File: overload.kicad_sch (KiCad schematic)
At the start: 50 parts, among them J1 AudioPlug2, J2 AudioPlug4, Q1 NPN, Q10 NPN, Q11 PNP, Q12 PNP, Q13 NPN, Q14 NPN, Q15 PNP, Q16 PNP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

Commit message: feat: updated footprint tables
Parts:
- C1, C2: footprint (none) -> Capacitor_SMD:C_0603_1608Metric
- R1, R10, R11, R12, R13, R14, R15, R16, R17, R18, R19, R2, R20, R21, R22, R23, R3, R4, R5, R6, R7, R8, R9: footprint (none) -> Resistor_SMD:R_0603_1608Metric
- U1: footprint (none) -> NE5532DR:D8
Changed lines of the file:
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@@
 			)
 		)
-		(property "Footprint" ""
+		(property "Footprint" "Resistor_SMD:R_0603_1608Metric"
 			(at 145.542 124.46 90)
 			(effects
@@
 			)
 		)
-		(property "Footprint" ""
+		(property "Footprint" "Resistor_SMD:R_0603_1608Metric"
 			(at 223.012 99.06 90)
 			(effects
@@
 			)
 		)
-		(property "Footprint" ""
+		(property "Footprint" "Resistor_SMD:R_0603_1608Metric"
 			(at 214.122 45.72 90)
 			(effects
@@
 			)
 		)
-		(property "Footprint" ""
+		(property "Footprint" "Resistor_SMD:R_0603_1608Metric"
 			(at 242.062 96.52 90)
 			(effects
@@
 			)
 		)
-		(property "Footprint" ""
+		(property "Footprint" "Capacitor_SMD:C_0603_1608Metric"
 			(at 94.2848 96.52 0)
 			(effects
@@
 			)
 		)
-		(property "Footprint" ""
+		(property "Footprint" "Capacitor_SMD:C_0603_1608Metric"
 			(at 99.06 71.4248 0)
 			(effects
@@
 			)
 		)
-		(property "Footprint" ""
+		(property "Footprint" "NE5532DR:D8"
 			(at 118.11 96.52 0)
 			(effects
@@
 			)
 		)
-		(property "Footprint" ""
+		(property "Footprint" "Resistor_SMD:R_0603_1608Metric"
 			(at 85.09 109.728 90)
 			(effects
@@
 			)
 		)
-		(property "Footprint" ""
+		(property "Footprint" "Resistor_SMD:R_0603_1608Metric"
 			(at 153.162 58.42 90)
 			(effects
@@
 			)
 		)
-		(property "Footprint" ""
+		(property "Footprint" "Resistor_SMD:R_0603_1608Metric"
 			(at 242.062 83.82 90)
 			(effects
@@
 			)
 		)
-		(property "Footprint" ""
+		(property "Footprint" "NE5532DR:D8"
 			(at 43.18 123.19 0)
 			(effects
@@
 			)
 		)
-		(property "Footprint" ""
+		(property "Footprint" "Resistor_SMD:R_0603_1608Metric"
 			(at 85.09 84.328 90)
 			(effects
@@
 			)
 		)
-		(property "Footprint" ""
+		(property "Footprint" "Resistor_SMD:R_0603_1608Metric"
 			(at 197.612 125.73 90)
 			(effects
@@
 			)
 		)
-		(property "Footprint" ""
+		(property "Footprint" "Resistor_SMD:R_0603_1608Metric"
 			(at 223.012 86.36 90)
 			(effects
@@
 			)
 		)
-		(property "Footprint" ""
+		(property "Footprint" "Resistor_SMD:R_0603_1608Metric"
 			(at 136.652 78.74 90)
 			(effects
@@
 			)
 		)
-		(property "Footprint" ""
+		(property "Footprint" "Resistor_SMD:R_0603_1608Metric"
 			(at 257.302 93.98 90)
 			(effects
@@
 			)
 		)
-		(property "Footprint" ""
+		(property "Footprint" "Resistor_SMD:R_0603_1608Metric"
 			(at 162.052 86.36 90)
 			(effects
@@
 			)
 		)
-		(property "Footprint" ""
+		(property "Footprint" "Resistor_SMD:R_0603_1608Metric"
 			(at 93.472 90.17 90)
 			(effects
@@
 			)
 		)
-		(property "Footprint" ""
+		(property "Footprint" "Resistor_SMD:R_0603_1608Metric"
 			(at 162.052 124.46 90)
 			(effects
@@
 			)
 		)
-		(property "Footprint" ""
+		(property "Footprint" "Resistor_SMD:R_0603_1608Metric"
 			(at 257.302 86.36 90)
 			(effects
@@
 			)
 		)
-		(property "Footprint" ""
+		(property "Footprint" "Resistor_SMD:R_0603_1608Metric"
 			(at 105.41 84.328 90)
 			(effects
@@
 			)
 		)
-		(property "Footprint" ""
+		(property "Footprint" "Resistor_SMD:R_0603_1608Metric"
 			(at 145.542 86.36 90)
 			(effects
@@
 			)
 		)
-		(property "Footprint" ""
+		(property "Footprint" "Resistor_SMD:R_0603_1608Metric"
 			(at 169.672 102.87 90)
 			(effects
@@
 			)
 		)
-		(property "Footprint" ""
+		(property "Footprint" "NE5532DR:D8"
 			(at 63.5 93.98 0)
 			(effects
@@
 			)
 		)
-		(property "Footprint" ""
+		(property "Footprint" "Resistor_SMD:R_0603_1608Metric"
 			(at 177.8 98.298 90)
 			(effects
@@
 			)
 		)
-		(property "Footprint" ""
+		(property "Footprint" "Resistor_SMD:R_0603_1608Metric"
 			(at 214.122 125.73 90)
 			(effects
@@
 			)
 		)
-		(property "Footprint" ""
+		(property "Footprint" "Resistor_SMD:R_0603_1608Metric"
 			(at 105.41 109.728 90)
 			(effects
@@
 			)
 		)
-		(property "Footprint" ""
+		(property "Footprint" "Resistor_SMD:R_0603_1608Metric"
 			(at 206.502 67.31 90)
 			(effects

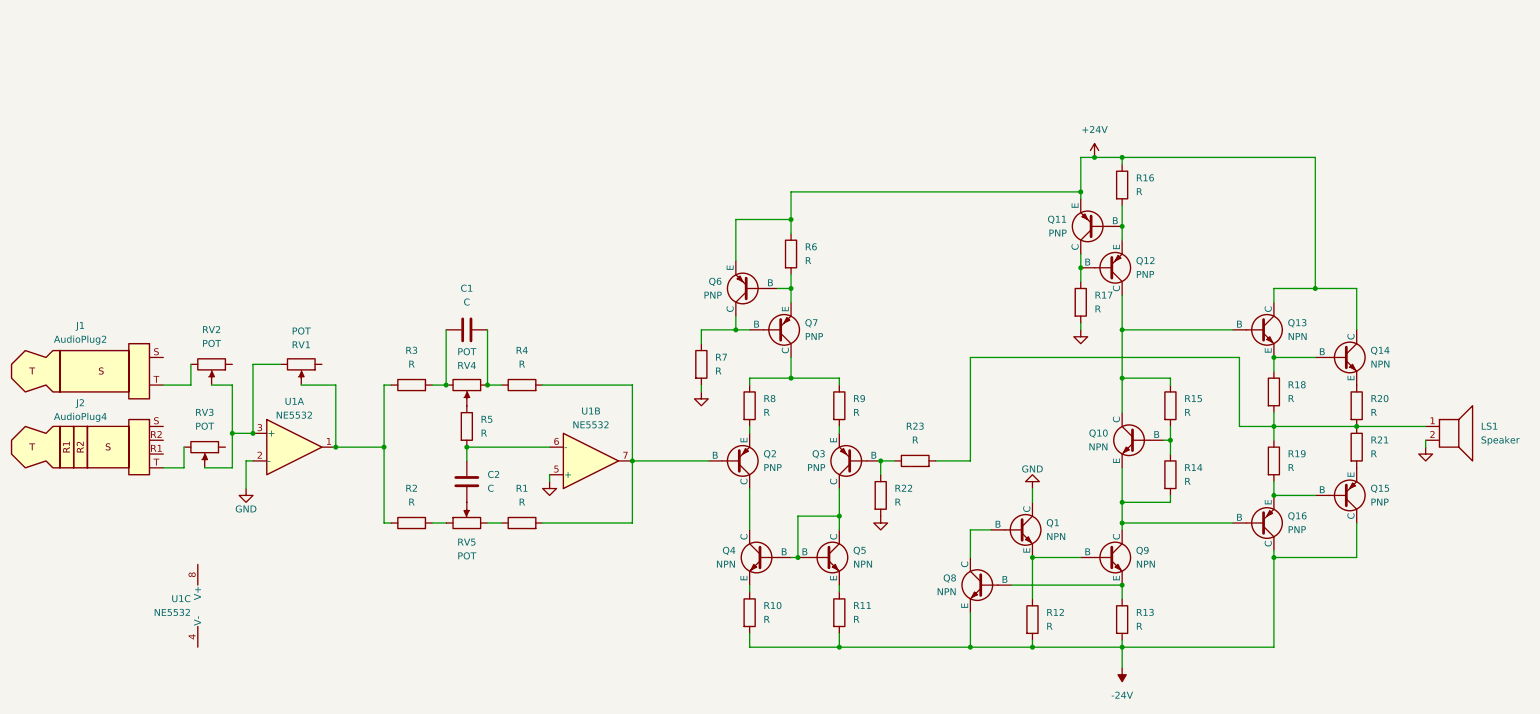
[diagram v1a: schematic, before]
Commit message: organize the schematic and add status led
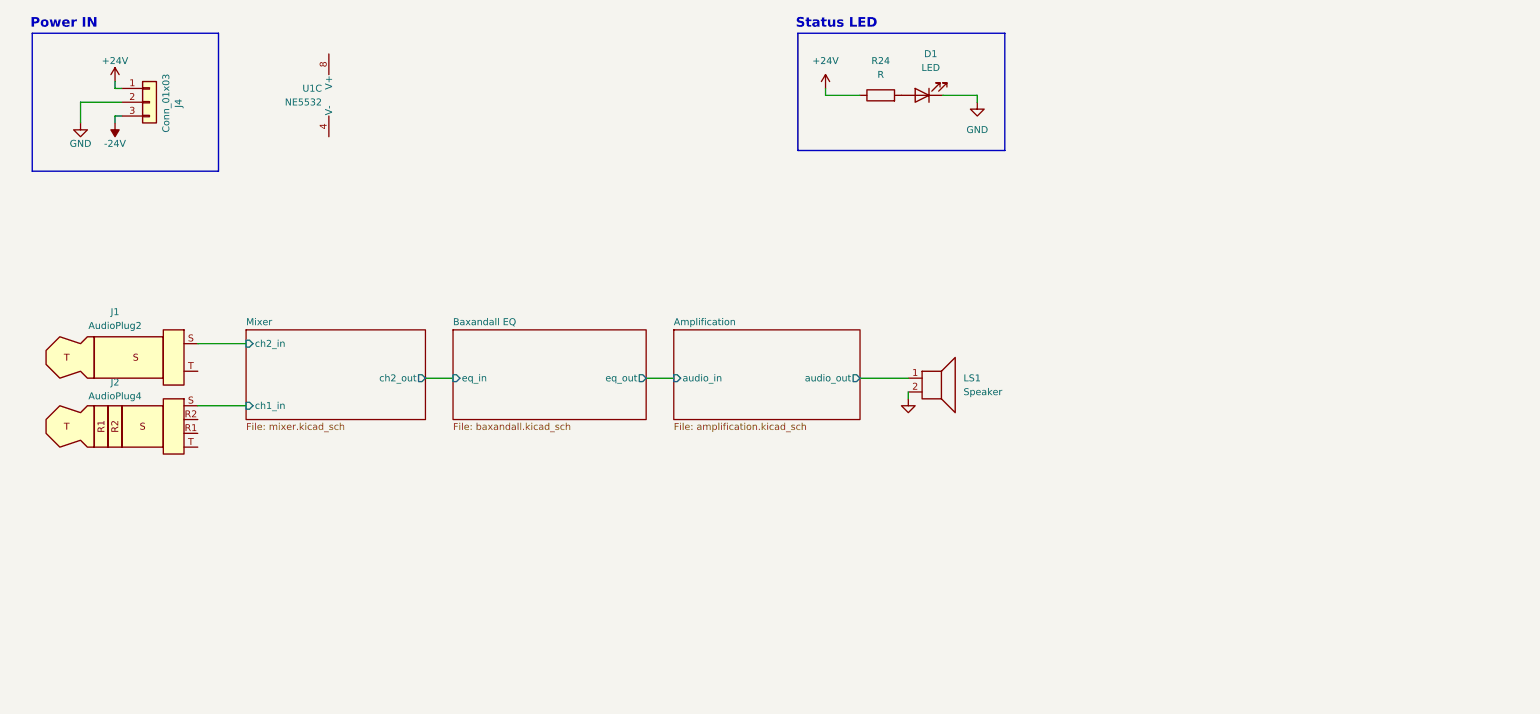
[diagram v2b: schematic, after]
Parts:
- removed C1, C2: C, Capacitor_SMD:C_0603_1608Metric, symbol Device:C
- removed Q1, Q10, Q13, Q14, Q4, Q5, Q8, Q9: NPN, symbol Simulation_SPICE:NPN
- removed Q11, Q12, Q15, Q16, Q2, Q3, Q6, Q7: PNP, symbol Simulation_SPICE:PNP
- removed R1, R10, R11, R12, R13, R14, R15, R16, R17, R18, R19, R2, R20, R21, R22, R23, R3, R4, R5, R6, R7, R8, R9: R, Resistor_SMD:R_0603_1608Metric, symbol Device:R
- removed RV1, RV2, RV3, RV4, RV5: POT, symbol Eagle_Main:POT
- removed unit 2 of U1
- removed unit 1 of U1
- added D1: LED, symbol Device:LED
- added J4: Conn_01x03, symbol Connector_Generic:Conn_01x03
- added R24: R, symbol Device:R
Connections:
- net +24V: now also J4.1 (Pin_1), R24.1
- net -24V: now also J4.3 (Pin_3)
- net GND: now also D1.1 (K), J4.2 (Pin_2)
- net Mixer/ch2_in: now reaches J1.S
- net Amplification/audio_out: now reaches LS1.1
- net Mixer/ch1_in: now reaches J2.S
- new net: D1.2 (A), R24.2
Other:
- added sheet Amplification (amplification.kicad_sch)
- added sheet Baxandall EQ (baxandall.kicad_sch)
- added sheet Mixer (mixer.kicad_sch)
- note added: "Power IN"
- note added: "Status LED"
- moved on the sheet: J1, J2, LS1, U1C

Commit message: add gnd to audio jacks
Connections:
- net GND: now also J1.T, J2.T
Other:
- sheet Mixer ports: added mixer_out; removed ch2_out
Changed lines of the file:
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@@
+	(wire
+		(pts
+			(xy 45.72 93.98) (xy 49.53 93.98)
+		)
+		(stroke
+			(width 0)
+			(type default)
+		)
+	)
 	(wire
 		(pts
@@
 		(pts
 			(xy 24.13 30.48) (xy 31.75 30.48)
+		)
+		(stroke
+			(width 0)
+			(type default)
+		)
+	)
+	(wire
+		(pts
+			(xy 45.72 80.01) (xy 49.53 80.01)
 		)
 		(stroke
@@
 	)
 	(symbol
+		(lib_id "power:GND")
+		(at 49.53 93.98 0)
+		(unit 1)
+		(exclude_from_sim no)
+		(in_bom yes)
+		(on_board yes)
+		(dnp no)
+		(property "Reference" "#PWR016"
+			(at 49.53 100.33 0)
+			(effects
+				(font
+					(size 1.27 1.27)
+				)
+				(hide yes)
+			)
+		)
+		(property "Value" "GND"
+			(at 49.53 97.79 0)
+			(effects
+				(font
+					(size 1.27 1.27)
+				)
+			)
+		)
+		(property "Footprint" ""
+			(at 49.53 93.98 0)
+			(effects
+				(font
+					(size 1.27 1.27)
+				)
+				(hide yes)
+			)
+		)
+		(property "Datasheet" ""
+			(at 49.53 93.98 0)
+			(effects
+				(font
+					(size 1.27 1.27)
+				)
+				(hide yes)
+			)
+		)
+		(property "Description" "Power symbol creates a global label with name \"GND\" , ground"
+			(at 49.53 93.98 0)
+			(effects
+				(font
+					(size 1.27 1.27)
+				)
+				(hide yes)
+			)
+		)
+		(pin "1"
+		)
+		(instances
+			(project "overload"
+				(path "/113207a7-390c-4dda-b902-7923a2c1c4b8"
+					(reference "#PWR016")
+					(unit 1)
+				)
+			)
+		)
+	)
+	(symbol
 		(lib_id "Connector_Audio:AudioPlug2")
 		(at 30.48 77.47 0)
@@
 		)
 	)
+	(symbol
+		(lib_id "power:GND")
+		(at 49.53 80.01 0)
+		(unit 1)
+		(exclude_from_sim no)
+		(in_bom yes)
+		(on_board yes)
+		(dnp no)
+		(property "Reference" "#PWR015"
+			(at 49.53 86.36 0)
+			(effects
+				(font
+					(size 1.27 1.27)
+				)
+				(hide yes)
+			)
+		)
+		(property "Value" "GND"
+			(at 49.53 83.82 0)
+			(effects
+				(font
+					(size 1.27 1.27)
+				)
+			)
+		)
+		(property "Footprint" ""
+			(at 49.53 80.01 0)
+			(effects
+				(font
+					(size 1.27 1.27)
+				)
+				(hide yes)
+			)
+		)
+		(property "Datasheet" ""
+			(at 49.53 80.01 0)
+			(effects
+				(font
+					(size 1.27 1.27)
+				)
+				(hide yes)
+			)
+		)
+		(property "Description" "Power symbol creates a global label with name \"GND\" , ground"
+			(at 49.53 80.01 0)
+			(effects
+				(font
+					(size 1.27 1.27)
+				)
+				(hide yes)
+			)
+		)
+		(pin "1"
+		)
+		(instances
+			(project ""
+				(path "/113207a7-390c-4dda-b902-7923a2c1c4b8"
+					(reference "#PWR015")
+					(unit 1)
+				)
+			)
+		)
+	)
 	(sheet
 		(at 92.71 72.39)
@@
 			)
 		)
-		(pin "ch2_out" output
+		(pin "mixer_out" output
 			(at 87.63 81.28 0)
 			(effects

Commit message: initial component placement in pcb
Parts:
- D1: footprint (none) -> LED_THT:LED_D5.0mm
- J4: footprint (none) -> TerminalBlock:TerminalBlock_MaiXu_MX126-5.0-03P_1x03_P5.00mm
- LS1: footprint (none) -> TerminalBlock:TerminalBlock_MaiXu_MX126-5.0-02P_1x02_P5.00mm
- R24: footprint (none) -> Resistor_THT:R_Axial_DIN0207_L6.3mm_D2.5mm_P7.62mm_Horizontal
- U1: footprint NE5532DR:D8 -> NE5532DR:D8-M
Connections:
- net Amplification/audio_out renamed Amplification/amp_out
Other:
- sheet Amplification ports: added amp_in, amp_out; removed audio_in, audio_out
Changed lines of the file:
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@@
 			)
 		)
-		(property "Footprint" "NE5532DR:D8"
+		(property "Footprint" "NE5532DR:D8-M"
 			(at 67.31 29.21 0)
 			(effects
@@
 			)
 		)
-		(property "Footprint" ""
+		(property "Footprint" "TerminalBlock:TerminalBlock_MaiXu_MX126-5.0-02P_1x02_P5.00mm"
 			(at 181.61 86.36 0)
 			(effects
@@
 			)
 		)
-		(property "Footprint" ""
+		(property "Footprint" "LED_THT:LED_D5.0mm"
 			(at 179.07 29.21 0)
 			(effects
@@
 			)
 		)
-		(property "Footprint" ""
+		(property "Footprint" "Resistor_THT:R_Axial_DIN0207_L6.3mm_D2.5mm_P7.62mm_Horizontal"
 			(at 171.45 30.988 90)
 			(effects
@@
 			)
 		)
-		(property "Footprint" ""
+		(property "Footprint" "TerminalBlock:TerminalBlock_MaiXu_MX126-5.0-03P_1x03_P5.00mm"
 			(at 36.83 30.48 0)
 			(effects
@@
 			)
 		)
-		(pin "audio_out" output
+		(pin "amp_out" output
 			(at 167.64 81.28 0)
 			(effects
@@
 			)
 		)
-		(pin "audio_in" input
+		(pin "amp_in" input
 			(at 133.35 81.28 180)
 			(effects

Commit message: feat: updated schematic
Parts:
- J1: footprint (none) -> TRS625:TRS
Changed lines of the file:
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@@
 			)
 		)
-		(property "Footprint" ""
+		(property "Footprint" "TRS625:TRS"
 			(at 39.37 78.74 0)
 			(effects

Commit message: feat: assigned footprint to symb
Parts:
- J2: footprint (none) -> TRS625:325 jack
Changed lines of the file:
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@@
 			)
 		)
-		(property "Footprint" ""
+		(property "Footprint" "TRS625:325 jack"
 			(at 39.37 91.44 0)
 			(effects

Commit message: RAAAAH Let's gooo to production baby
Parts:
- removed J2: AudioPlug4, TRS625:325 jack, symbol Connector_Audio:AudioPlug4
- added J3: AudioPlug3, TRS625:325 jack, symbol Connector_Audio:AudioPlug3
- added R22, R23: R, Resistor_THT:R_Axial_DIN0207_L6.3mm_D2.5mm_P7.62mm_Horizontal, symbol Device:R
- added U2: LM7812_TO220, Package_TO_SOT_THT:TO-220-3_Vertical, symbol Regulator_Linear:LM7812_TO220
- added U3: LM7912_TO220, Package_TO_SOT_THT:TO-220-3_Vertical, symbol Regulator_Linear:LM7912_TO220
- U1: footprint NE5532DR:D8-M -> Package_DIP:DIP-8_W7.62mm_Socket
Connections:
- net +24V: now also J4.3 (Pin_3), U2.1 (VI); no longer J4.1 (Pin_1)
- net -24V: now also J4.1 (Pin_1), U3.2 (VI); no longer J4.3 (Pin_3)
- net GND: now also J1.S, J3.S, U2.2 (GND), U3.1 (GND); no longer J1.T
- net Mixer/ch1_in: now also R22.2, R23.2
- net Mixer/ch2_in: now also J1.T; no longer J1.S
- net at U1.4 (V-): now also U3.3 (VO)
- net at U1.8 (V+): now also U2.3 (VO)
- new net: J3.T, R22.1
- new net: J3.R, R23.1
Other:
- note added: "Opamp Supply"
- moved on the sheet: J1, LS1, U1C

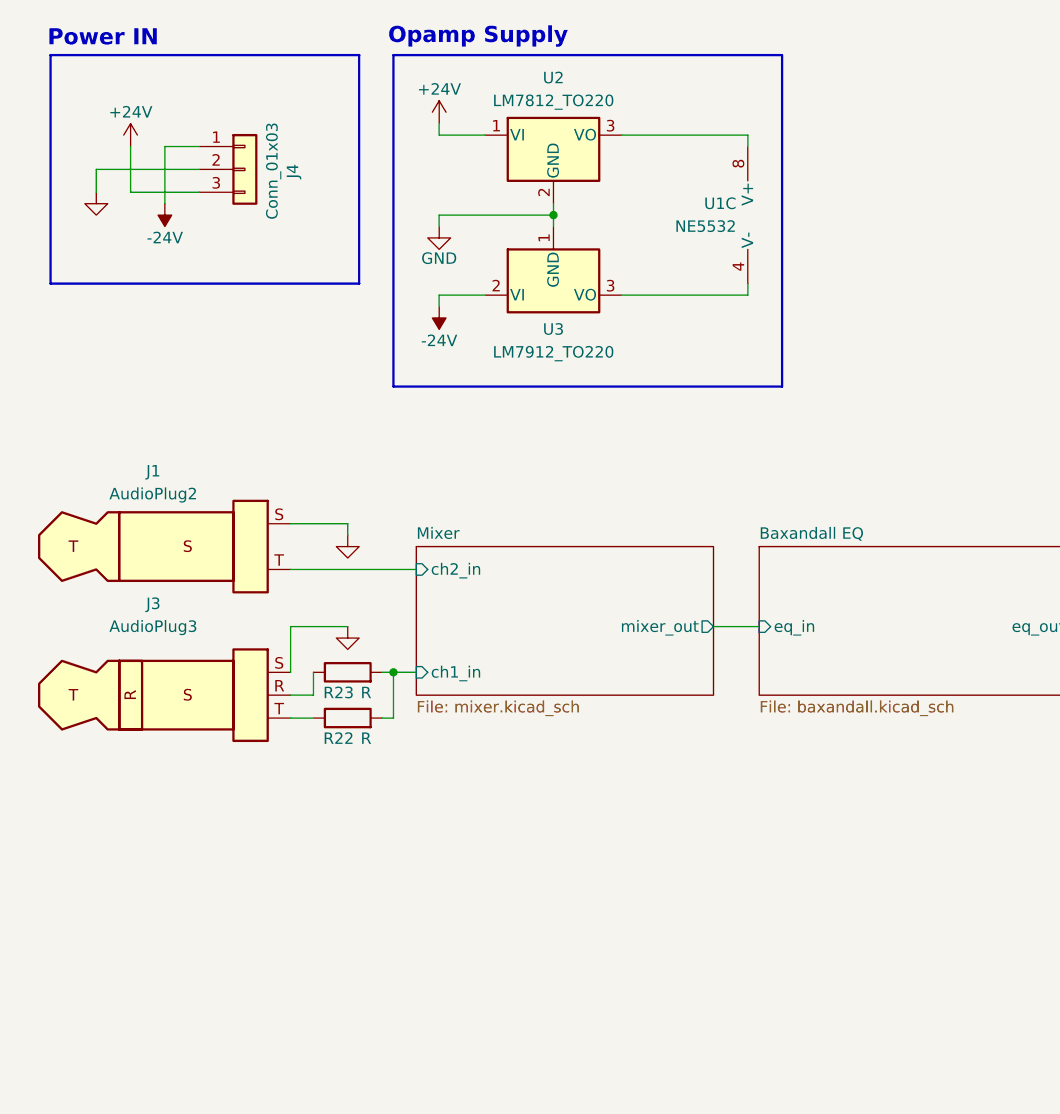
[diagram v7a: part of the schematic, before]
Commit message: remove mask on high current tracks
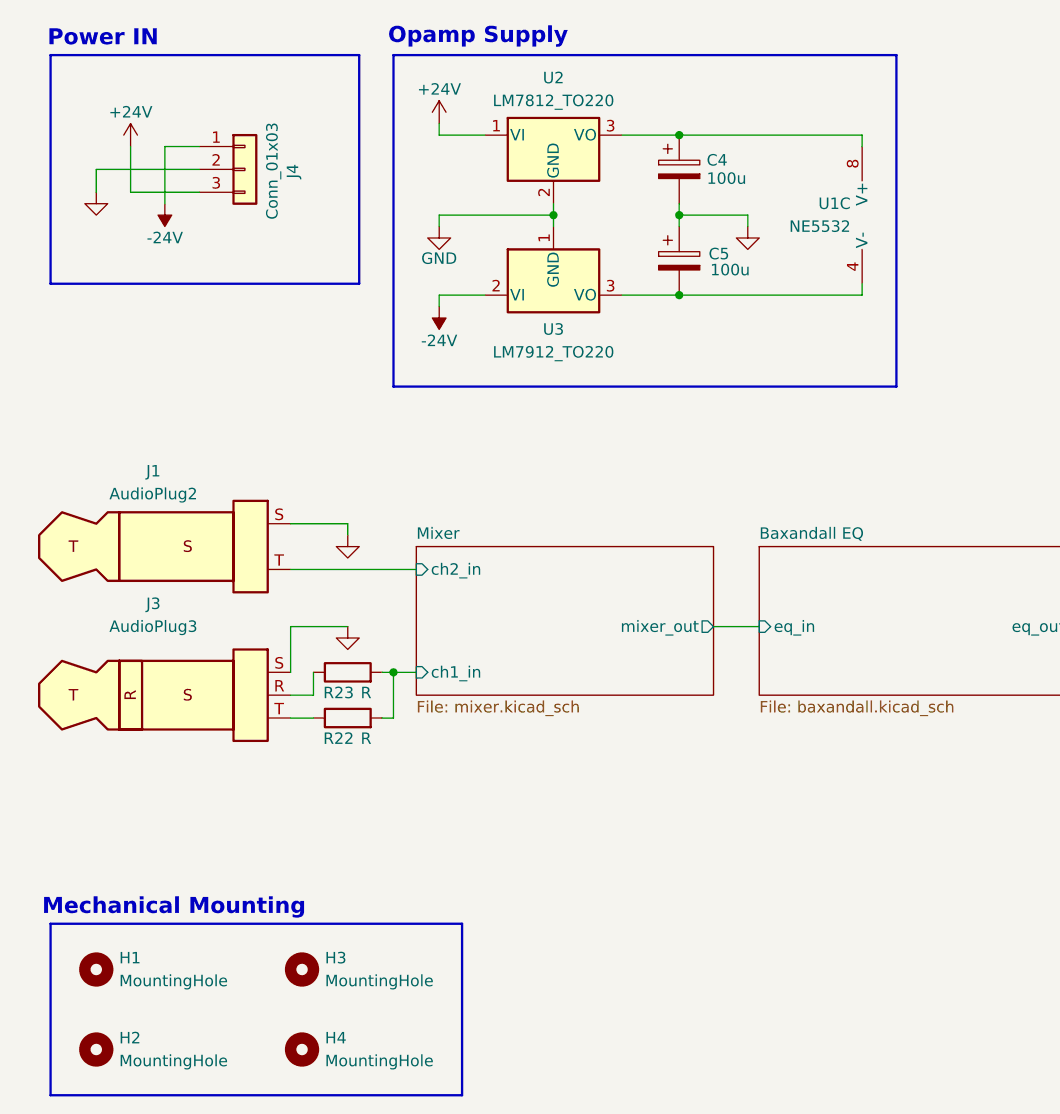
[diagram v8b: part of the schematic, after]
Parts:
- added C4, C5: 100u, Capacitor_THT:CP_Radial_D6.3mm_P2.50mm, symbol Device:C_Polarized
- added H1, H2, H3, H4: MountingHole, MountingHole:MountingHole_4.3mm_M4, symbol Mechanical:MountingHole
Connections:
- net GND: now also C4.2, C5.1
- net at U1.8 (V+), U2.3 (VO): now also C4.1
- net at U1.4 (V-), U3.3 (VO): now also C5.2
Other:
- note added: "Mechanical Mounting"
- moved on the sheet: U1C
